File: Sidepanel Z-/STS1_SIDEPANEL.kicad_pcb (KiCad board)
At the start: 2 copper layers, 98 x 98 mm, 62 parts, among them IC1 TMP112AQDRLRQ1, J1 Conn_01x08, J3 Conn_02x02_Odd_Even, U1 GUVA-C32SM, U11 INA180A4, U12 INA180A4

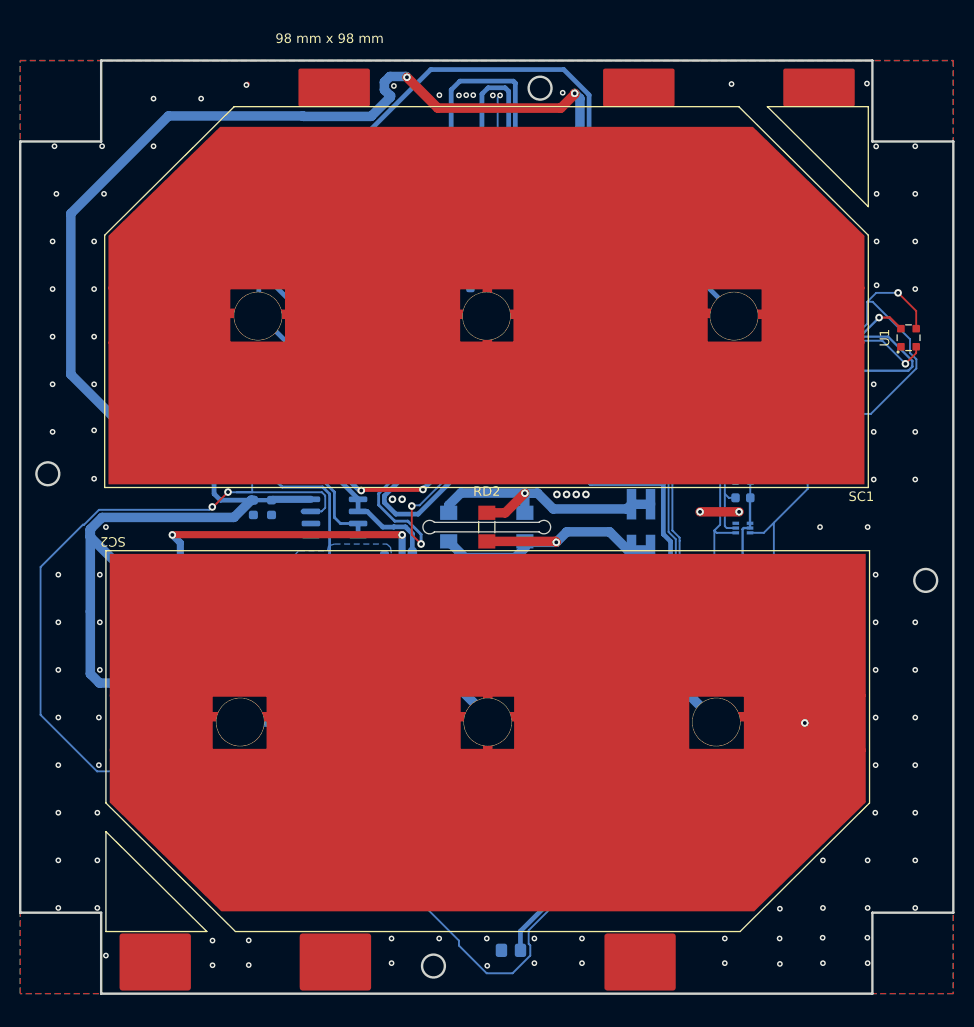
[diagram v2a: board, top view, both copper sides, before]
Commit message: Changed the layout of all the sidepanel PCBs to mitigate the problems that arised from the bad previous design.
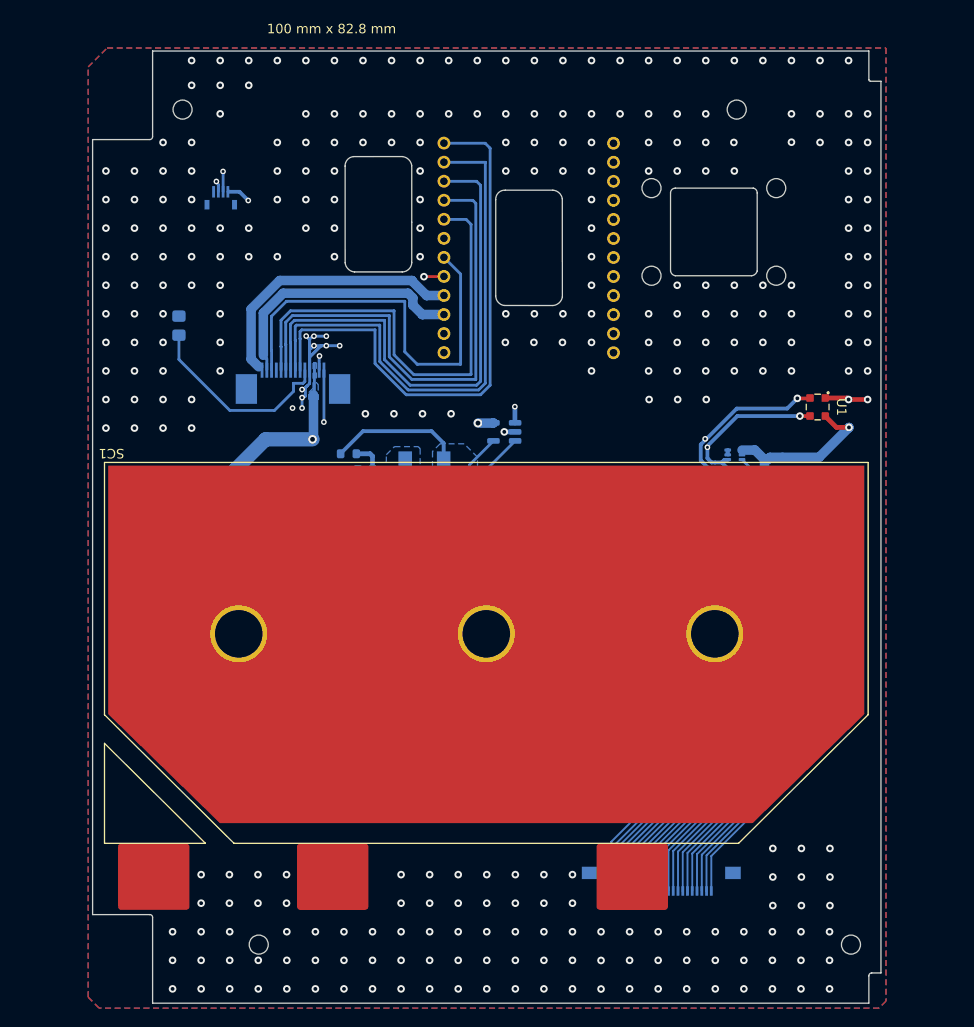
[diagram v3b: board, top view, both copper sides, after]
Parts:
- removed C2, CF1, CF2: 1u, Capacitor_SMD:C_0603_1608Metric
- removed C22: 1n, Capacitor_SMD:C_0603_1608Metric
- removed COUT11, COUT12: 4u7, Capacitor_SMD:C_0603_1608Metric
- removed COUT21, COUT22, C_CUR21, C_CUR22, C_IN1, C_IN2: 10u, Capacitor_SMD:C_0603_1608Metric
- removed CUR1, CUR2: TMCS1101A3BQDT, Package_SO:SOIC-8_3.9x4.9mm_P1.27mm
- removed C_41, C_42, C_CUR11, C_CUR12: 100n, Capacitor_SMD:C_0603_1608Metric
- removed D1, D2: PMEG2020EH, Diode_SMD:D_SOD-123F
- removed DOUT2: SMM4F5.0, SamacSys:STMITE
- removed J1: Conn_01x08, STS_Connector:SAMTEC_ZF5S-08-01-T-WT
- removed L_IN1, L_IN2: 10u, STS_Inductor_SMD:XAL6060103MEC
- removed MPPT2: SPV1040TTR, Package_SO:TSSOP-8_4.4x3mm_P0.65mm
- removed R12: 1M, Resistor_SMD:R_0603_1608Metric
- removed R22: 330k, Resistor_SMD:R_0603_1608Metric
- removed R32, RF11, RF12, RF21, RF22: 1k, Resistor_SMD:R_0603_1608Metric
- removed R42: 0, Resistor_SMD:R_0603_1608Metric
- removed R52: 10m, Resistor_SMD:R_0603_1608Metric
- removed RD1, RD2, RD3: 22R, Resistor_SMD:R_MiniMELF_MMA-0204
- removed RIC1, RIC2: 4k7, Resistor_SMD:R_0603_1608Metric
- removed RS1, RS2: 0R01, Resistor_SMD:R_0603_1608Metric
- removed SC2: Solar_Cell, STS_solder:3G30A_40x80_Z_SC2
- removed U12: INA180A4, Package_TO_SOT_SMD:SOT-23-5
- added C11: 10u, Capacitor_SMD:C_0603_1608Metric, B.Cu at (120.8, 89.5)
- added C31: 1n, Capacitor_SMD:C_0603_1608Metric, B.Cu at (107.8, 88.7)
- added C41: 4u7, Capacitor_SMD:C_0603_1608Metric, B.Cu at (114.9, 91.1)
- added C51: 1u, Capacitor_SMD:C_0603_1608Metric, B.Cu at (104.8, 86.2)
- added C61: 10u, Capacitor_SMD:C_0603_1608Metric, B.Cu at (109.7, 93.3)
- added D11: PMEG2020EH, Diode_SMD:D_SOD-123F, B.Cu at (114.6, 89.0)
- added J2: Conn_01x16, STS_connector:SAMTEC_ZF5S-14-01-T-WT, B.Cu at (104.6, 75.0)
- added L1: 10u, STS_Inductor_SMD:IND_XAL6060-103MEC, B.Cu at (118.5, 84.3)
- added R61: 1M, Resistor_SMD:R_0603_1608Metric, B.Cu at (105.2, 89.6)
- added R71: 330k, Resistor_SMD:R_0603_1608Metric, B.Cu at (103.7, 89.6)
- added cam1: 54548-2271, STS_connector:545482271, B.Cu at (148.9, 111.0)
- added edu_con1: 54548-2271, STS_connector:545482271, B.Cu at (143.3, 125.7)
- added uci_conn: conn_to_panel, STS_connector:conn_to_panel, F.Cu at (138.3, 71.2)
- C21: value 1n -> 100n
- D21: renamed from DOUT1; footprint SamacSys:STMITE -> STS_semiconductor:DIO_SMM4F5.0A-TR
- J3: value Conn_02x02_Odd_Even -> Conn_01x12; footprint STS_Connector:M808280442 -> STS_connector:conn_to_panel; moved to F.Cu
- Outline1: footprint USER_OUTLINE:OUTLINE_SidepanelZ+ -> STS_Sidepanels_Outline:OUTLINE_SidepanelZ-
- R11: value 1M -> 10m
- R21: value 330k -> 1k
- R41: value 0 -> 1k
- R51: value 10m -> 0R01
- SC1: footprint STS_solder:3G30A_40x80_Z_SC1 -> STS_solder:3G30A_40x80
- U1: footprint STS_UV:OLGA 2mm x 2,3mm -> STS_UV:OLGA
- UV1: footprint STS_Connector:5014610491 -> STS_connector:5014610491
- moved TH1 74.3 mm to (92.7, 68.3), turned to 90 degrees
- moved UV1 68.7 mm to (97.1, 55.2), turned to 180 degrees
- moved SC1 37.4 mm to (124.9, 102.7), turned to 180 degrees
- moved D21 34.9 mm to (113.3, 93.2)
- moved R21 32.2 mm to (110.5, 81.8), turned to 180 degrees
- moved C21 29.4 mm to (112.2, 83.5), turned to 0 degrees
- moved J3 27.6 mm to (120.5, 71.2), turned to 90 degrees
- moved R11 27.6 mm to (124.0, 84.8), turned to 180 degrees
- moved MPPT1 27.4 mm to (110.2, 86.1), turned to 180 degrees
- moved R31 26.5 mm to (102.5, 85.4), turned to 0 degrees
- moved R51 16.9 mm to (110.8, 91.0)
- moved R41 14.2 mm to (102.5, 86.9), turned to 0 degrees
- moved U11 12.6 mm to (126.8, 79.5), turned to 180 degrees
- moved U1 12.0 mm to (159.8, 76.9), turned to -90 degrees
- moved RU2 9.03 mm to (150.5, 86.3)
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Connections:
- C21 pad 1: Net-(C21-Pad1) -> GND
- C21 pad 2: GND -> Net-(MPPT1-MPP-SET)
- J3 pad 1: /AntennaDeployment/ANT_DEPLOY+ -> unconnected-(J3-Pin_1-Pad1)
- J3 pad 2: /AntennaDeployment/ANT_DEPLOY+ -> unconnected-(J3-Pin_2-Pad2)
- J3 pad 3: /AntennaDeployment/ANT_DEPLOY- -> /Bat-
- J3 pad 4: /AntennaDeployment/ANT_DEPLOY- -> /Bat+
- MPPT1 pad 1: Net-(C_41-Pad2) -> Net-(MPPT1-MPP-SET)
- MPPT1 pad 5: Net-(C21-Pad1) -> Net-(MPPT1-VCTRL)
- MPPT1 pad 6: Net-(CF1-Pad1) -> Net-(MPPT1-ICTRL_MINUS)
- MPPT1 pad 7: Net-(CF1-Pad2) -> Net-(MPPT1-ICTRL_PLUS)
- MPPT1 pad 8: Net-(C_41-Pad2) -> Net-(MPPT1-MPP-SET)
- R11 pad 1: Net-(C21-Pad1) -> /SC1_V+
- R11 pad 2: /MPPT1 -> /SolarMPPT/CUR1_OUT
- R21 pad 1: GND -> Net-(MPPT1-MPP-SET)
- R21 pad 2: Net-(C21-Pad1) -> /SolarMPPT/CUR1_OUT
- R31 pad 1: Net-(C_41-Pad2) -> /SolarMPPT/MPPT1_OUT
- R31 pad 2: /SolarMPPT/CUR1_OUT(1) -> Net-(MPPT1-ICTRL_PLUS)
- R41 pad 1: /SC1_V+ -> /MPPT1
- R41 pad 2: /SolarMPPT/CUR1_OUT -> Net-(MPPT1-ICTRL_MINUS)
- R51 pad 1: /SolarMPPT/CUR1_OUT -> /MPPT1
- R51 pad 2: /SolarMPPT/CUR1_OUT(1) -> /SolarMPPT/MPPT1_OUT
- U11 pad 3: /SolarMPPT/CUR1_OUT -> /SC1_V+
- U11 pad 4: /SolarMPPT/CUR1_OUT(1) -> /SolarMPPT/CUR1_OUT
- UV1 pad 4: GND -> unconnected-(UV1-Pad4)
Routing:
- net /SC2_V+: track 222.4 -> 0.00 mm, vias 1 -> 0
- net /MPPT2: track 222.4 -> 0.00 mm, vias 2 -> 0
- net /SC2_I+: track 213.1 -> 0.00 mm, vias 2 -> 0
- net /SC1_V+: track 241.6 -> 78.4 mm, vias 2 -> 1
- net /TEMP+: track 83.6 -> 20.9 mm
- net /UART_RX: track 0.00 -> 59.4 mm
- net /UART_TX: track 0.00 -> 57.5 mm
- net /SolarMPPT/MPPT2_OUT: track 56.9 -> 0.00 mm, vias 2 -> 0
- net /COBC_SWDIO: track 0.00 -> 55.0 mm
- net /COBC_SWDCLK: track 0.00 -> 52.6 mm
- net /COBC_NOT_RST: track 0.00 -> 49.9 mm
- net /BAT_MIDDLE: track 0.00 -> 44.0 mm
- net /SDA: track 47.9 -> 91.5 mm, vias 1 -> 3
- net GND: track 71.6 -> 31.8 mm, vias 109 -> 332
- net /MPPT1: track 112.3 -> 79.5 mm, vias 0 -> 4
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- added copper zone on B.Cu, net /MPPT1
- added copper zone on B.Cu, net /SC1_V+
- added copper zone on B.Cu, net /SolarMPPT/CUR1_OUT
- added copper zone on In1.Cu, net GND
- added copper zone on In2.Cu, net GND
- removed copper zone on B.Cu, net /SolarMPPT/CUR1_OUT(1)
- removed copper zone on B.Cu, net /SolarMPPT/CUR2_OUT(1)
- removed copper zone on B.Cu, net /SolarMPPT/MPPT2_IN
- removed copper zone on B.Cu, net /SolarMPPT/MPPT2_OUT
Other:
- board size 98 x 98 mm -> 82.8 x 100 mm
- copper layers 2 -> 4
- board text added: "100 mm x 82.8 mm"
- board text removed: "98 mm x 98 mm"

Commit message: Added a  separate ground for the EDU  sensors and did  some small changes for ordering.
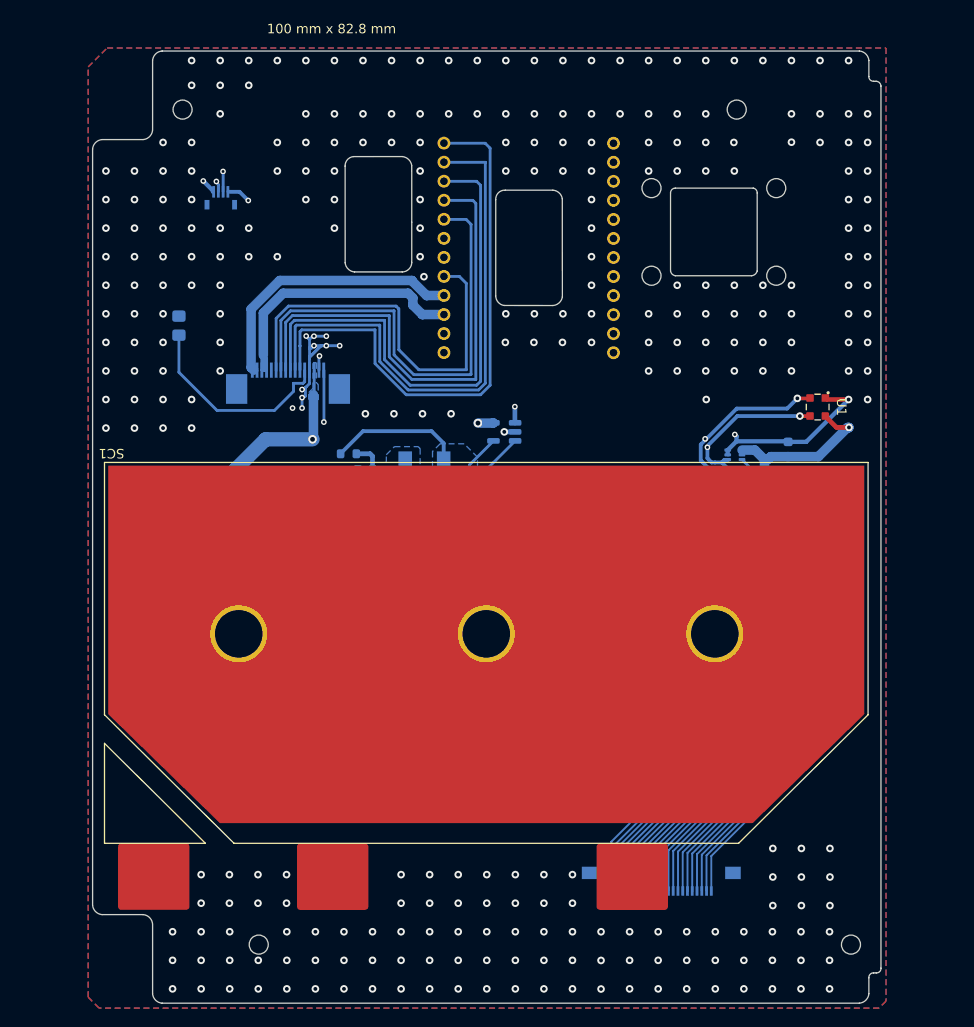
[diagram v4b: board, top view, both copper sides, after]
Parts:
- removed J2: Conn_01x16, STS_connector:SAMTEC_ZF5S-14-01-T-WT
- added J1: Conn_01x18, STS_connector:SAMTEC_ZF5S-16-01-T-WT, B.Cu at (104.1, 75.0)
- moved C1 1.73 mm to (156.7, 81.3), turned to 90 degrees
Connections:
- C1 pad 2: GND -> GND1
- IC1 pad 2: GND -> GND1
- IC1 pad 3: GND -> GND1
- J3 pad 10: /COBC_SWDIO -> /COBC_NOT_RST
- J3 pad 5: GND -> +5V
- J3 pad 6: /BAT_MIDDLE -> GND
- J3 pad 7: unconnected-(J3-Pin_7-Pad7) -> GND
- J3 pad 8: /COBC_NOT_RST -> /COBC_SWDCLK
- J3 pad 9: /COBC_SWDCLK -> /COBC_SWDIO
- U1 pad 1: GND -> GND1
- UV1 pad 4: unconnected-(UV1-Pad4) -> GND1
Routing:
- net GND1: track 0.00 -> 88.5 mm, vias 0 -> 3
- net /BAT_MIDDLE: track 44.0 -> 0.00 mm
- net +5V: track 0.00 -> 43.0 mm
- net GND: track 31.8 -> 21.4 mm, vias 332 -> 325
- net /COBC_NOT_RST: track 49.9 -> 55.0 mm
- net /Bat-: track 27.4 -> 31.1 mm
- net /COBC_SWDCLK: track 52.6 -> 49.9 mm
- net /COBC_SWDIO: track 55.0 -> 52.6 mm
- net /TEMP+: track 20.9 -> 21.7 mm
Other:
- outline, holes or cut-outs redrawn

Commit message: Commit before the order.
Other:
- board text added: "Z- V2.5"
- board text removed: "Z-"
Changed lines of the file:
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@@
       (drillshape 0)
       (scaleselection 1)
-      (outputdirectory "../Gerber/X+/")
+      (outputdirectory "../../gerber_SIDEPANELS/Z-/")
     )
   )
@@
     )
   )
-  (gr_text "Z-" (at 91.98 41.24) (layer "B.SilkS")
+  (gr_text "Z- V2.5\n" (at 94.6 41.8) (layer "B.SilkS")
     (effects (font (size 1 1) (thickness 0.15)))
   )
@@
   (segment (start 123.935788 74.6) (end 116.95 74.6) (width 0.3) (layer "B.Cu") (net 51))
   (segment (start 120.5096 53.1866) (end 123.9366 53.1866) (width 0.3) (layer "B.Cu") (net 51))
-  (segment (start 102.875 73.02) (end 102.875 67.582106) (width 0.3) (layer "B.Cu") (net 52))
-  (segment (start 117.8634 72.975) (end 122.85 72.975) (width 0.3) (layer "B.Cu") (net 52))
-  (segment (start 122.85 72.975) (end 122.85 63.9) (width 0.3) (layer "B.Cu") (net 52))
-  (segment (start 102.875 67.582106) (end 104.170505 66.2866) (width 0.3) (layer "B.Cu") (net 52))
-  (segment (start 122.125 63.175) (end 120.5 63.175) (width 0.3) (layer "B.Cu") (net 52))
-  (segment (start 115.7634 66.579493) (end 115.7634 70.875) (width 0.3) (layer "B.Cu") (net 52))
-  (segment (start 122.85 63.9) (end 122.125 63.175) (width 0.3) (layer "B.Cu") (net 52))
-  (segment (start 115.470507 66.2866) (end 115.7634 66.579493) (width 0.3) (layer "B.Cu") (net 52))
-  (segment (start 115.7634 70.875) (end 117.8634 72.975) (width 0.3) (layer "B.Cu") (net 52))
-  (segment (start 104.170505 66.2866) (end 115.470507 66.2866) (width 0.3) (layer "B.Cu") (net 52))
+  (segment (start 102.775 67.540682) (end 102.775 71.475) (width 0.5) (layer "B.Cu") (net 52))
+  (segment (start 104.165684 66.15) (end 102.775 67.540682) (width 0.5) (layer "B.Cu") (net 52))
+  (segment (start 122.75 72.875) (end 117.573528 72.875) (width 0.5) (layer "B.Cu") (net 52))
+  (segment (start 102.875 71.575) (end 102.775 71.475) (width 0.3) (layer "B.Cu") (net 52))
+  (segment (start 122.125 63.175) (end 122.75 63.8) (width 0.5) (layer "B.Cu") (net 52))
+  (segment (start 115.475328 66.15) (end 104.165684 66.15) (width 0.5) (layer "B.Cu") (net 52))
+  (segment (start 117.573528 72.875) (end 115.8634 71.164872) (width 0.5) (layer "B.Cu") (net 52))
+  (segment (start 102.775 71.475) (end 102.775 71.77) (width 0.5) (layer "B.Cu") (net 52))
+  (segment (start 115.8634 71.164872) (end 115.8634 66.538072) (width 0.5) (layer "B.Cu") (net 52))
+  (segment (start 115.8634 66.538072) (end 115.475328 66.15) (width 0.5) (layer "B.Cu") (net 52))
+  (segment (start 120.5 63.175) (end 122.125 63.175) (width 0.5) (layer "B.Cu") (net 52))
+  (segment (start 122.75 63.8) (end 122.75 72.875) (width 0.5) (layer "B.Cu") (net 52))
+  (segment (start 102.875 73.02) (end 102.875 71.575) (width 0.3) (layer "B.Cu") (net 52))
   (zone (net 1) (net_name "GND") (layers "F&B.Cu") (name "gnd") (hatch edge 0.5)
     (connect_pads (clearance 0))
